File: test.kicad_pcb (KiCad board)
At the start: 2 copper layers, 97.5 x 72.5 mm, 20 parts, among them P1 CONN_02X20, P10 CONN_01X01, P11 CONN_01X04, P12 CONN_01X05, P13 CONN_01X05, P14 CONN_01X05, P15 CONN_01X04, P16 CONN_01X04, P17 CONN_01X04, P2 CONN_02X04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

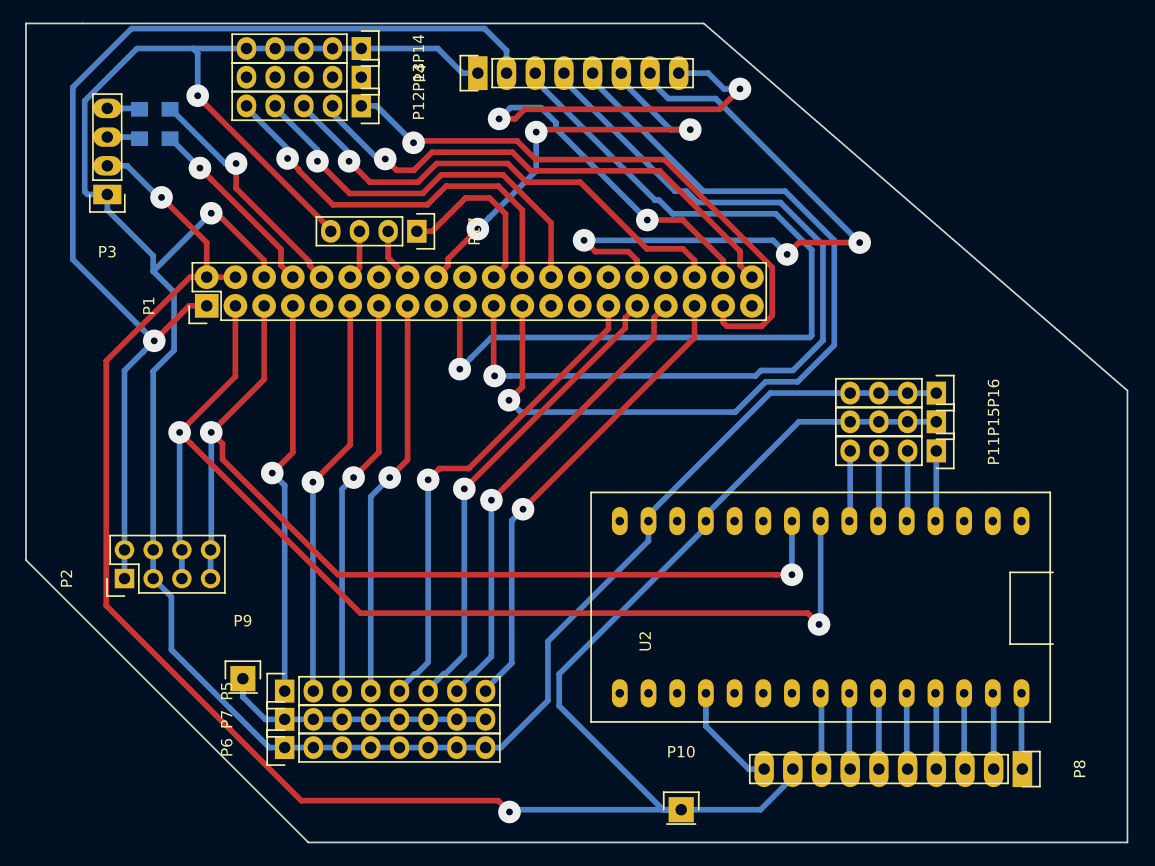
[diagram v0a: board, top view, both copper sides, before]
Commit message: Input channel count increased in hardware, but not in software
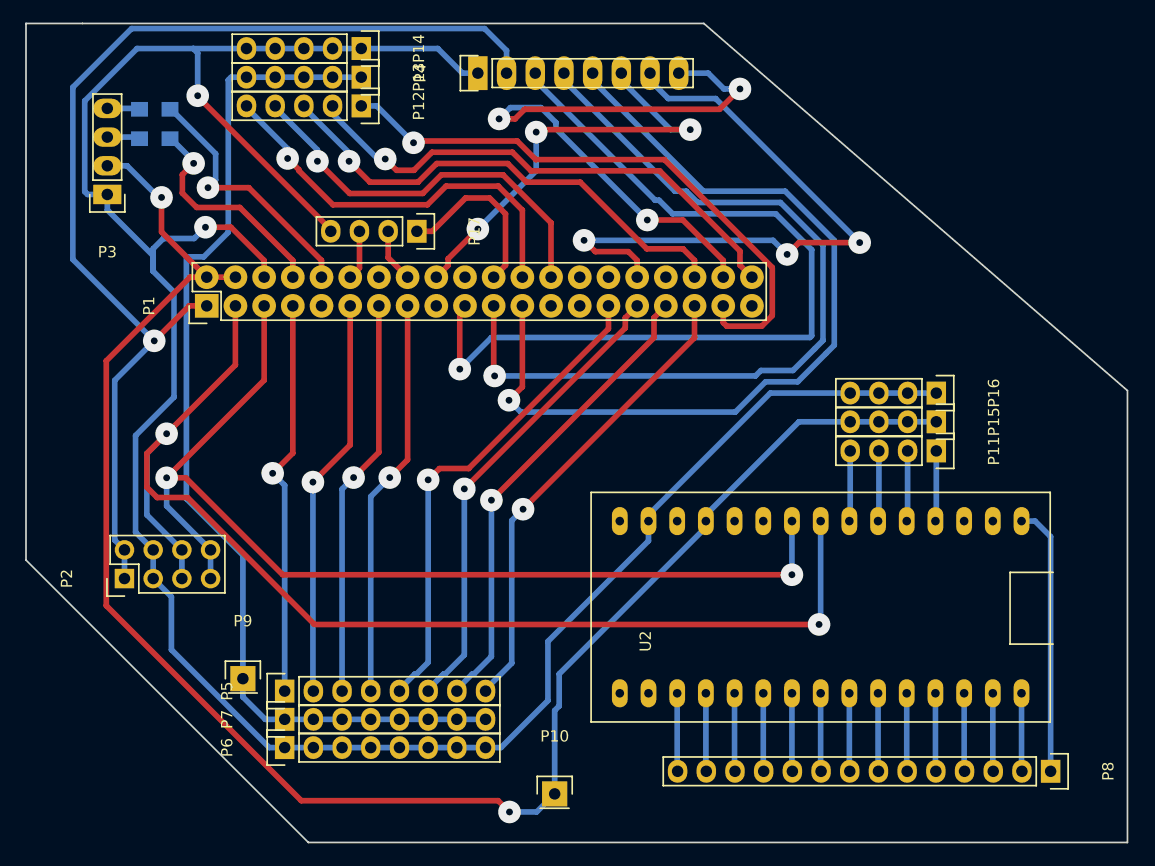
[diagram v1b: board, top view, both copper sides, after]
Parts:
- P8: value CONN_01X10 -> CONN_01X14; footprint Pin_Headers:Pin_Header_Straight_1x10 -> Pin_Headers:Pin_Header_Straight_1x14
- moved P10 11.3 mm to (176.8, 173.2)
- moved P8 2.51 mm to (220.7, 171.2)
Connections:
- P8 pad 9: /5V -> Net-(P8-Pad9)
- U2 pad 11: (no net) -> Net-(P8-Pad11)
- U2 pad 13: (no net) -> Net-(P8-Pad10)
- U2 pad 15: Net-(P8-Pad8) -> Net-(P8-Pad9)
- U2 pad 17: Net-(P8-Pad7) -> Net-(P8-Pad8)
- U2 pad 19: Net-(P8-Pad6) -> Net-(P8-Pad7)
- U2 pad 21: Net-(P8-Pad5) -> Net-(P8-Pad6)
- U2 pad 23: Net-(P8-Pad4) -> Net-(P8-Pad5)
- U2 pad 25: Net-(P8-Pad3) -> Net-(P8-Pad4)
- U2 pad 27: Net-(P8-Pad2) -> Net-(P8-Pad3)
- U2 pad 29: Net-(P8-Pad1) -> Net-(P8-Pad2)
- U2 pad 30: (no net) -> Net-(P8-Pad1)
- U2 pad 5: (no net) -> Net-(P8-Pad14)
- U2 pad 7: Net-(P8-Pad10) -> Net-(P8-Pad13)
- U2 pad 9: (no net) -> Net-(P8-Pad12)
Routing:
- net /RAIL: track 23.9 -> 93.3 mm
- net /5V: track 181.9 -> 153.1 mm
- net Net-(P8-Pad1): track 6.74 -> 23.9 mm
- net /SDA: track 99.1 -> 107.9 mm
- net Net-(P8-Pad9): track 0.00 -> 7.03 mm
- net Net-(P8-Pad14): track 0.00 -> 6.92 mm
- net Net-(P8-Pad13): track 0.00 -> 6.92 mm
- net Net-(P8-Pad12): track 0.00 -> 6.92 mm
- net Net-(P8-Pad11): track 0.00 -> 6.92 mm
- net /SCL: track 88.3 -> 93.0 mm
- net /TXD: track 16.8 -> 19.9 mm
- net Net-(P8-Pad10): track 9.64 -> 6.92 mm
- net /RXD: track 21.0 -> 23.1 mm
- net /GND: track 217.0 -> 218.5 mm
- net /3V3: track 96.8 -> 97.6 mm

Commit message: Status leds added to hardware
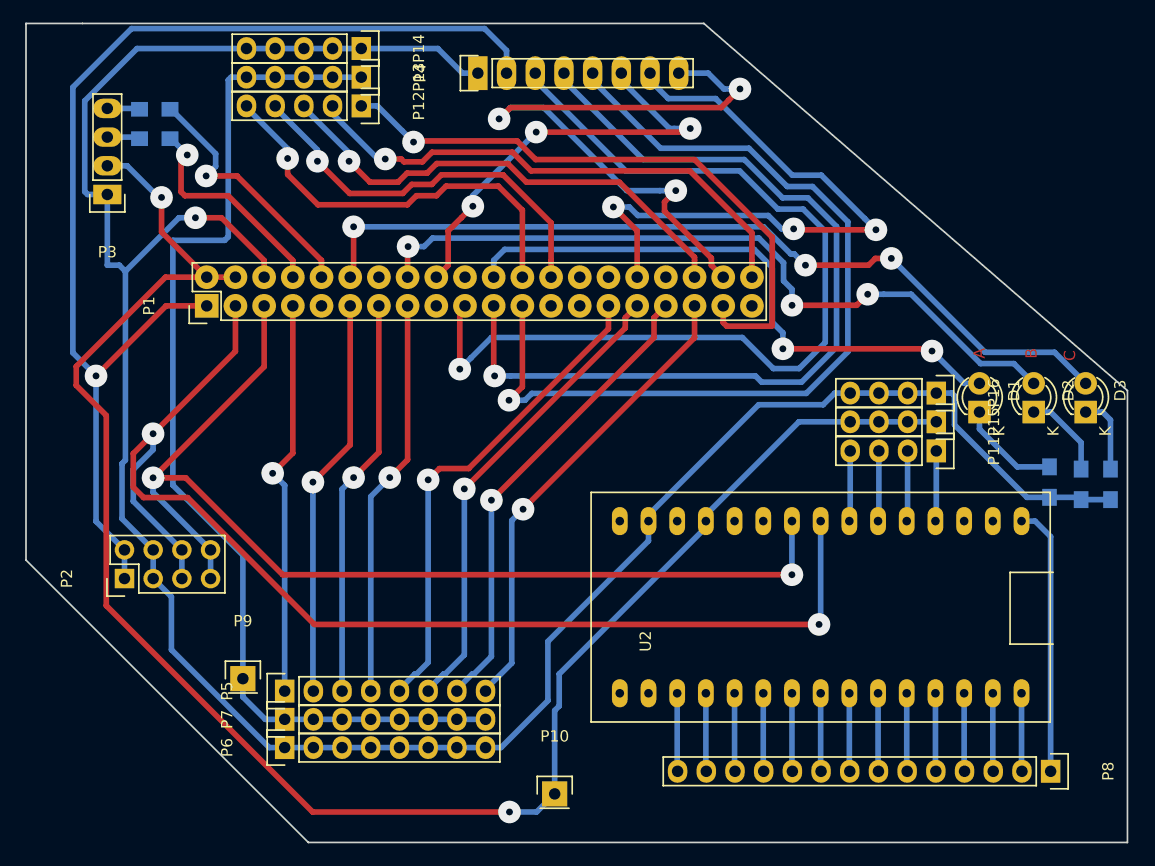
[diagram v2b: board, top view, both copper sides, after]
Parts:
- removed P17: CONN_01X04, Pin_Headers:Pin_Header_Straight_1x04
- added D1: LED, LEDs:LED-3MM, F.Cu at (214.4, 139.4)
- added D2: LED, LEDs:LED-3MM, F.Cu at (219.2, 139.4)
- added D3: LED, LEDs:LED-3MM, F.Cu at (223.8, 139.4)
- added R3: R, Resistors_SMD:R_0805_HandSoldering, B.Cu at (220.6, 145.6)
- added R4: R, Resistors_SMD:R_0805_HandSoldering, B.Cu at (223.4, 145.8)
- added R5: R, Resistors_SMD:R_0805_HandSoldering, B.Cu at (226.0, 145.8)
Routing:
- net /STATUS_C: track 4.40 -> 75.6 mm, vias 0 -> 3
- net /STATUS_B: track 4.77 -> 66.3 mm, vias 0 -> 3
- net /STATUS_A: track 15.7 -> 53.5 mm, vias 0 -> 2
- net Net-(D1-Pad1): track 0.00 -> 9.09 mm
- net Net-(D2-Pad1): track 0.00 -> 7.67 mm
- net Net-(D3-Pad1): track 0.00 -> 6.84 mm
- net /MOSI: track 77.1 -> 83.1 mm
- net /MISO: track 74.7 -> 78.8 mm
- net /3V3: track 97.6 -> 101.1 mm
- net /5V: track 153.1 -> 156.3 mm
- net /SCLK: track 77.7 -> 80.5 mm
- net /RAIL: track 93.3 -> 96.1 mm
- net /SCL: track 93.0 -> 95.2 mm
- net /SDA: track 107.9 -> 110.1 mm
- net /AUX0: track 53.1 -> 55.1 mm
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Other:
- board text added: "A"
- board text added: "B"
- board text added: "C"

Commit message: Bugs fixed, added 5v connector
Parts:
- added P17: CONN_01X02, Pin_Headers:Pin_Header_Straight_1x02, F.Cu at (134.8, 129.2)
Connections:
- P8 pad 14: Net-(P8-Pad14) -> /5V
- U2 pad 5: Net-(P8-Pad14) -> (no net)
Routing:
- net /5V: track 156.3 -> 174.0 mm, vias 2 -> 3
- net Net-(P8-Pad14): track 6.92 -> 0.00 mm
- net /GND: track 218.1 -> 222.8 mm
- net /RAIL: track 96.1 -> 93.0 mm
- net /SCL: track 95.2 -> 92.6 mm
- net /3V3: track 101.1 -> 102.7 mm
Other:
- board text added: "0"
- board text added: "1"
- board text added: "10"
- board text added: "11"
- board text added: "2"
- board text added: "3"
- board text added: "4"
- board text added: "5"
- board text added: "5V"
- board text added: "6"
- board text added: "7"
- board text added: "8"
- board text added: "9"
- board text added: "ADC"
- board text added: "AUX PWM"
- board text added: "Arduino Nano"
- board text added: "GND"
- board text added: "HRPI v1.2"
- board text added: "I2C"
- board text added: "RCIN"
- board text added: "RCOUT"
- board text added: "SPI"
- board text added: "Serial 5V"
- board text added: "USB CONN"

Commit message: Added board render
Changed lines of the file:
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@@
   (general
     (links 104)
-    (no_connects 2)
+    (no_connects 0)
     (area 129.924999 104.924999 227.575001 177.575001)
     (thickness 1.6)
-    (drawings 53)
+    (drawings 55)
     (tracks 504)
     (zones 0)
@@
     (pad 40 thru_hole oval (at 2.54 48.26 90) (size 2.1 2.1) (drill 1.016) (layers *.Cu *.Mask F.SilkS)
       (net 40 /AUX1))
+    (model /home/admin/Документы/PINS.x3d
+      (at (xyz 0.15 0.05 -0.456693))
+      (scale (xyz 10 10 10))
+      (rotate (xyz -90 0 0))
+    )
   )
   (module arduino:arduino_nano (layer F.Cu)
@@
     )
   )
+  (gr_text 1 (at 167.8 112.2) (layer F.Cu)
+    (effects (font (size 1 1) (thickness 0.25)))
+  )
+  (gr_text 1 (at 135 122) (layer F.Cu)
+    (effects (font (size 1 1) (thickness 0.25)))
+  )
   (gr_text 5V (at 131.2 129.6) (layer F.Cu)

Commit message: Updated README.md
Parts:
- added D5: LED, LEDs:LED-3MM, F.Cu at (183.2, 141.8)
- added R7: R, Resistors_SMD:R_0805_HandSoldering, B.Cu at (188.6, 140.0)
- R1, R2: value 7k -> 10k
- R3, R4, R5: value R -> 470
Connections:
- U2 pad 10: (no net) -> /RCOK
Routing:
- net /RCOK: track 0.00 -> 35.6 mm, vias 0 -> 2
- net Net-(D5-Pad1): track 0.00 -> 5.67 mm
- net /GND: track 222.8 -> 225.8 mm
- net /SDA: track 110.1 -> 109.4 mm
